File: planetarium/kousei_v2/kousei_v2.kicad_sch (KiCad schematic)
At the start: 40 parts, among them J13 Jack-DC, J2 Conn_01x03, J3 Conn_01x02, J4 Conn_01x02, J5 Conn_01x02, J6 Conn_01x02, J7 Conn_01x02, J8 Conn_01x02, U1 CL6808, U2 CL6808, U3 CL6808, U4 CL6808, U5 CL6808, U6 CL6808, U7 TC7WZ07FK, U8 R-78K5.0-2.0L

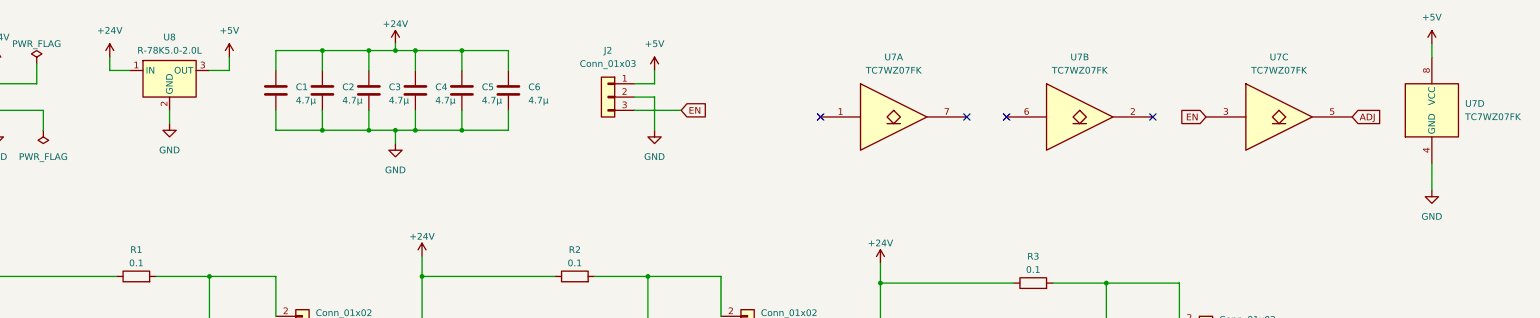
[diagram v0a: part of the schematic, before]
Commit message: change: LED追加, EN->nEN
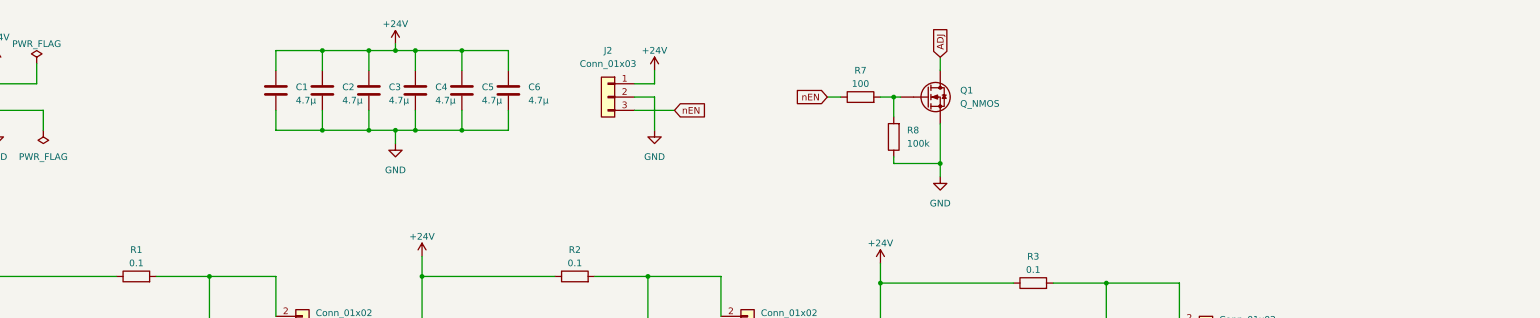
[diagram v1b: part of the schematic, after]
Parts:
- removed U7: TC7WZ07FK, TC7WZ07FK:TC7WZ07FK, symbol 74xGxx:74LVC3G07
- removed U8: R-78K5.0-2.0L, R-78K5.0-2.0L:R-78K5.0-2.0L, symbol Converter_DCDC:OKI-78SR-3.3_1.5-W36H-C
- added Q1: Q_NMOS, Package_TO_SOT_SMD:TSOT-23_HandSoldering, symbol Device:Q_NMOS
- added R7: 100, Resistor_SMD:R_0402_1005Metric, symbol Device:R
- added R8: 100k, Resistor_SMD:R_0402_1005Metric, symbol Device:R
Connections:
- net +5V is gone; now on net +24V: J2.1 (Pin_1)
- net ADJ: now also Q1.3 (D)
- net GND: now also Q1.2 (S), R8.1
- net EN renamed nEN
- net nEN: now also R7.1
- new net: Q1.1 (G), R7.2, R8.2
- no-connect marks 4 -> 0
